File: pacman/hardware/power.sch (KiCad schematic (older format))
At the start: 36 parts, among them Q4 RRR015P03TL, U3 PCF8574A, U4 INA_226, U5 ADS1115, U6 LTC3638, U7 NCS6S1205C, U8 Si8600, U9 NCP1117ST33T3G

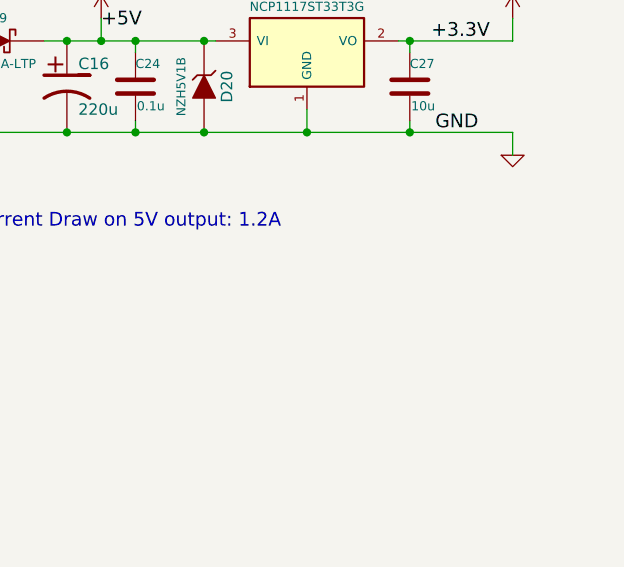
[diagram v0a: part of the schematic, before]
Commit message: Added in annotations about hardware changed
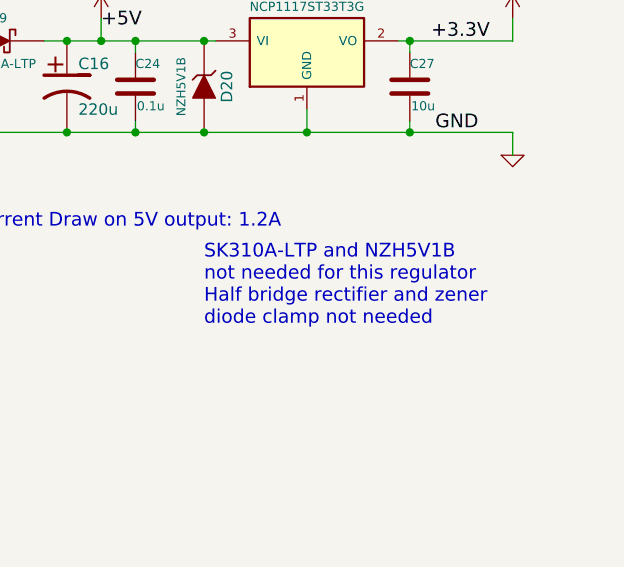
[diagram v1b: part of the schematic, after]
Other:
- note added: "SK310A-LTP and NZH5V1B\nnot needed for this regulator\nHalf bridge rectifier and zener\ndiode clamp not needed"
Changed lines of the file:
@@
 	1    0    0    -1
 $EndComp
+Text Notes 8700 6250 0    60   ~ 0
+SK310A-LTP and NZH5V1B\nnot needed for this regulator\nHalf bridge rectifier and zener\ndiode clamp not needed
 $EndSCHEMATC
